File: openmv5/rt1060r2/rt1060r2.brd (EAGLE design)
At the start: 35.6 x 44.5 mm, 254 parts, among them CN1 S2B-PH-K-S(LF)(SN), IC1 LM66200DRLR, IC2 TCR2LF33,LM_CT, IC3 AP61300Z6-7, IC4 IS42S16160G-6BL, IC5 IS25LP128F-JKLE-TR, IC6 ATECC608B-MAHDA-T, IC7 MXC4005XC, IC8 KSZ8081RNDCA-TR, IC9 MIMXRT106FCVL5B, J1 USB4105-GF-A, J2 USD-1040310811, J3 DF12-36-DS, J4 DNP, J5 DNP, J6 DNP, J7 DNP, J8 3221-10-0300-00, J9 DNP, M1 9774030151R, M2 9774030151R, Q1 DMG2301L-7, Q2 2N7002KW_R1_00001, Q3 2N7002KW_R1_00001, Q4 2N7002KW_R1_00001, U1 BQ24075RGTR, U2 LBEE5KL1DX-883, Y1 ECS-327MVATX-3-CN-TR3, Y2 XRCGB24M000F3M00R0, Y3 SC32S-7PF20PPM

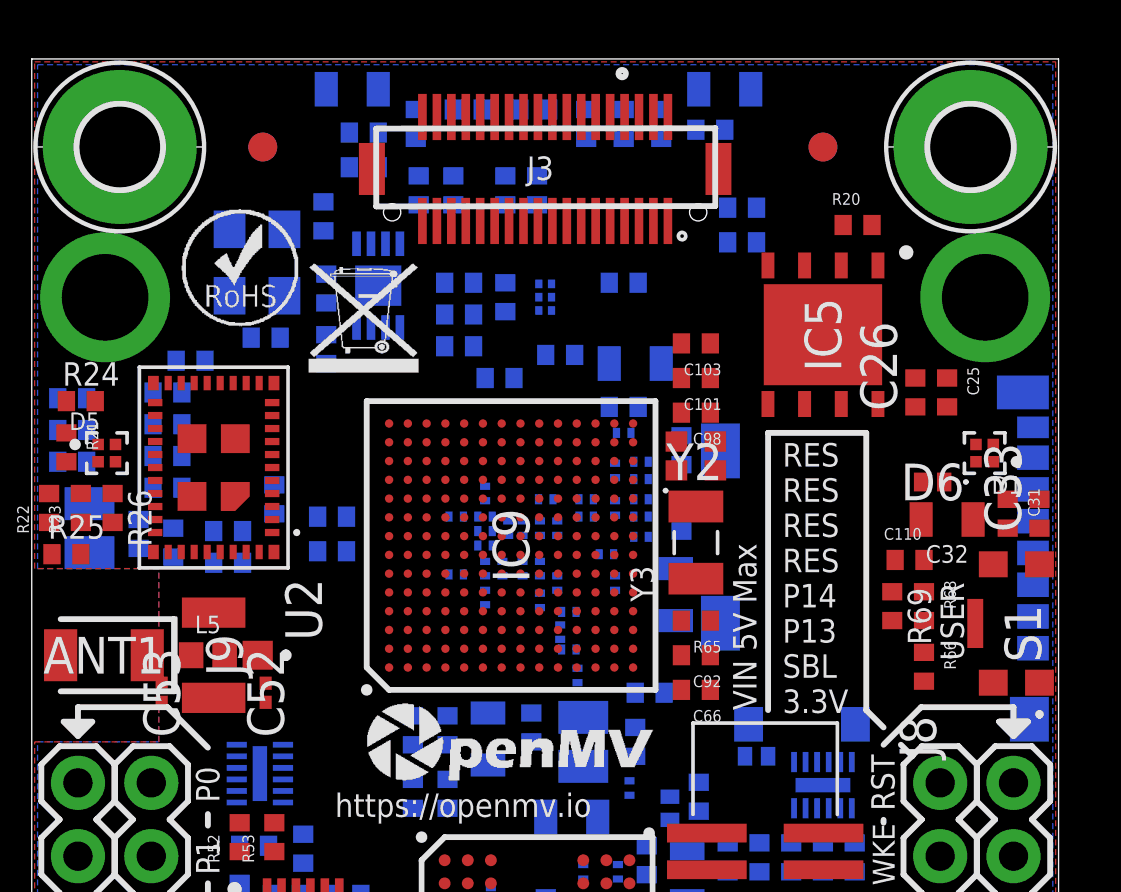
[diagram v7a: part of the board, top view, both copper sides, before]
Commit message: Update the Design with the new crypto chip
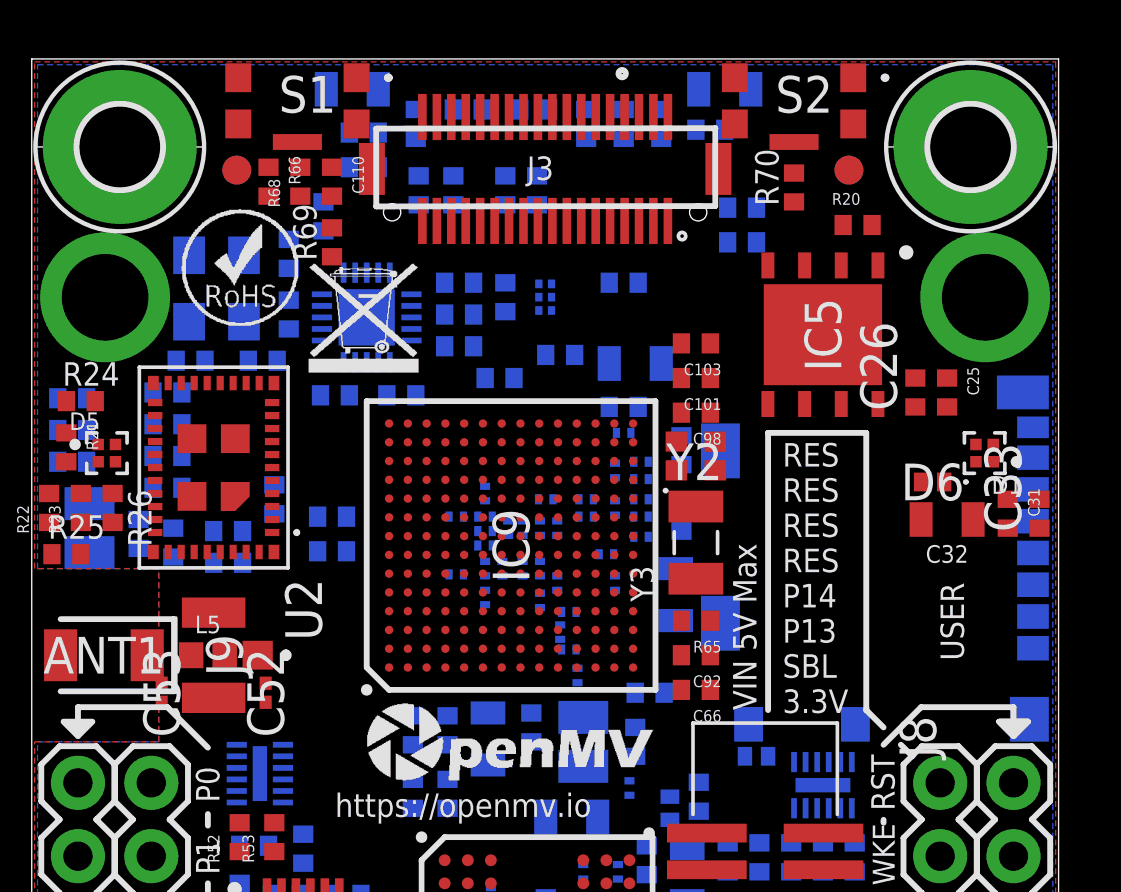
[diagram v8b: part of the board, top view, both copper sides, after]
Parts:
- added C111: 0.1uF, 0402:0402
- added C112: 4.7uF, 0402:0402
- added R70: 10K, 0402:0402
- added S2: KMS231GLFS, KMS231GLFS:KMS231GLFS
- IC6: value ATECC608B-MAHDA-T -> SE050C1HQ1_Z01SCZ; device ATECC608B-MAHDA-T:SON50P300X200X60-9N -> SE050C1HQ1_Z01SCZ:QFN40P300X300X33-21N
- moved S1 30.8 mm to (9.20, 43.0), turned to 180 degrees
- moved R66 28.2 mm to (8.20, 40.2)
- moved R68 26.1 mm to (9.30, 40.2), turned to 90 degrees
- moved C110 23.9 mm to (10.4, 40.2), turned to 270 degrees
- moved R69 23.1 mm to (10.4, 38.1), turned to 90 degrees
- moved C27 1.77 mm to (8.90, 37.7)
- moved C29 1.77 mm to (8.90, 35.6)
- moved Y1 1.66 mm to (6.40, 36.5)
- moved FD5 1.20 mm to (28.3, 40.6)
- moved FD7 1.20 mm to (28.3, 40.6)
- moved FD3 1.20 mm to (7.10, 40.6)
- moved FD6 1.20 mm to (7.10, 40.6)
- moved IC6 1.17 mm to (11.6, 35.5), turned to 0 degrees
- moved R47 0.81 mm to (8.00, 34.0)
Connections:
- new net C_VOUT: C111.1, C112.2, IC6.15, IC6.18
- new net RST_BUTTON: R70.2, S2.2, S2.3, S2.4
- net GND: now also C111.2, C112.1, IC6.19, IC6.21, S2.1, S2.5; no longer IC6.4, IC6.9
- net INT_I2C_SCL: now also IC6.10; no longer IC6.6
- net INT_I2C_SDA: now also IC6.9; no longer IC6.5
- net P12_RST_N: now also R70.1
- net VCC: now also IC6.11, IC6.12; no longer IC6.8
